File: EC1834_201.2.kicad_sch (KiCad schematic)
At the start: 69 parts, among them X4 Lautsprecher, X7 DB9_Female

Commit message: Page 1 & 2 connected Hierarchival connections created and tested
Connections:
- net 0: no longer R15.6 (R3.2)
- net 1: no longer R15.1 (R1.1)
- net 2: no longer R15.3 (R2.1)
- net 3: no longer R15.7 (R4.1)
- net 4: no longer R14.4 (R2.2)
- net 5: no longer R14.7 (R4.1)
- net 6: no longer R14.2 (R1.2)
- net 7: no longer R14.6 (R3.2)
- net A1: now also D85.14 (A3)
- net A14: now also D86.10 (B2)
- net A15: now also D86.6 (B1)
- net A16: now also D86.13 (B3)
- net A2: now also D85.5 (A1)
- net A3: now also D85.2 (A0)
- net A4: now also D85.11 (A2)
- net A5: now also D86.2 (A0)
- net A6: now also D86.11 (A2)
- net A7: now also D86.5 (A1)
- net A9: now also D85.13 (B3)
- net PS3:1: now also D60.10 (S), R52.8 (R7.2)
- net ~{DACK0}: now also D58.1 (R)
- net ~{MEMR}: now also BR1.1 (A)
- net ~{RAMADRSEL}: now also D87.9 (A4), D88.3 (Y1)
- net ADRSEL: now reaches D58.9, D67.2 (D), D85.1 (WS), D86.1 (WS)
- net A12: now reaches D85.10 (B2)
- net A11: now reaches D85.3 (B0)
- net A10: now reaches D85.6 (B1)
- net A13: now reaches D86.3 (B0)
- net at D57.10 (B3), D57.12 (A4), D57.13 (B4)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: now also D58.3 (C)
- net ~{MEMW}: now reaches D60.12 (D)
- net 5PW1: now reaches D60.13 (R)
- net 5PW1: now also D58.10 (S), D58.4 (S), D67.4 (S)
- net at D58.2 (D), D69.8 (Y3): now also D67.1 (R), D70.1 (A1), D70.4 (A2)
- net OSC1: now reaches D57.1 (A1), D57.2 (B1)
- net OSC: now reaches D57.8 (Y3)
- net at D67.5, D69.1 (A1): now also D69.12 (A4)
- new net MEM0: R15.6 (R3.2)
- new net MEM1: R15.1 (R1.1)
- new net MEM2: R15.3 (R2.1)
- new net MEM3: R15.7 (R4.1)
- new net MEM4: R14.4 (R2.2)
- new net MEM5: R14.7 (R4.1)
- new net MEM6: R14.2 (R1.2)
- new net MEM7: R14.6 (R3.2)
- no-connect marks 44 -> 45

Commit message: Completed BUS Final checks required
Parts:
- BR1, WD4, WD5: footprint (none) -> Resistor_THT:R_Axial_DIN0204_L3.6mm_D1.6mm_P7.62mm_Horizontal
- D10, D13, D16, D34, D37, D39, D47, D5, D52, D57, D58, D59, D60, D62, D63, D67, D68, D69, D70, D71, D72, D82, D87, D88, D90: footprint (none) -> Package_DIP:DIP-14_W7.62mm
- D100, D101, D115, D116: footprint (none) -> Package_DIP:DIP-28_W15.24mm
- D111, D112, D30, D31, D44: footprint (none) -> Package_DIP:DIP-20_W7.62mm
- D65, D66, D85, D86: footprint (none) -> Package_DIP:DIP-16_W7.62mm
- E4, X4: footprint (none) -> Connector_PinHeader_2.54mm:PinHeader_1x02_P2.54mm_Vertical
- L1: footprint (none) -> Package_DIP:DIP-8_W7.62mm
- PS3: footprint (none) -> Connector_PinHeader_2.54mm:PinHeader_1x09_P2.54mm_Vertical
- PS4: footprint (none) -> Connector_PinHeader_2.54mm:PinHeader_1x03_P2.54mm_Vertical
- X7: footprint (none) -> Connector_Dsub:DSUB-9_Female_Horizontal_P2.77x2.84mm_EdgePinOffset9.90mm_Housed_MountingHolesOffset11.32mm
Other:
- company: (none) -> Mario Gögel 2022
- title: EC1834_201.2 -> EC1834 Hauptplatine 201.2

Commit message: Small corrections on Page 201.1
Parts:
- WD4: value SolderJumper_2_Bridged -> SolderJumper_2_Open; symbol Jumper:SolderJumper_2_Bridged -> Jumper:SolderJumper_2_Open
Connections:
- net ~{MEMR} is gone; now on net PS4:1: BR1.1 (A), D60.3 (C)
- net ~{MEMADRSEL}: now also D90.3 (Y1), WD5.2 (B)
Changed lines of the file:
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@@
     (stroke (width 0) (type default) (color 0 0 0 0))
   )
-  (bus (pts (xy 134.62 271.78) (xy 134.62 275.59))
-    (stroke (width 0.5) (type default) (color 0 0 0 0))
-  )
   (wire (pts (xy 299.72 364.49) (xy 290.83 364.49))
     (stroke (width 0) (type default) (color 0 0 0 0))
@@
     (stroke (width 2) (type default) (color 0 0 0 0))
   )
-  (bus (pts (xy 138.43 223.52) (xy 138.43 226.06))
-    (stroke (width 0.5) (type default) (color 0 0 0 0))
-  )
   (wire (pts (xy 82.55 125.73) (xy 82.55 129.54))
     (stroke (width 0) (type default) (color 0 0 0 0))
@@
     (effects (font (size 1.27 1.27)) (justify left bottom))
   )
+  (label "~{MEMR}" (at 212.09 123.19 0)
+    (effects (font (size 1.27 1.27)) (justify left bottom))
+  )
   (label "~{OCHCK}" (at 172.72 316.23 0)
     (effects (font (size 1.27 1.27)) (justify left bottom))
@@
     (effects (font (size 1.27 1.27)) (justify left bottom))
   )
+  (label "~{MEMADRSEL}" (at 125.73 179.07 0)
+    (effects (font (size 1.27 1.27)) (justify left bottom))
+  )
   (label "PB1" (at 229.87 321.31 0)
     (effects (font (size 1.27 1.27)) (justify left bottom))
@@
   (symbol (lib_id "robotron_ec1834:DS8286D-D111") (at 156.21 217.17 0) (unit 1)
     (in_bom yes) (on_board yes)
-    (property "Reference" "D44" (id 0) (at 156.21 204.9018 0))
+    (property "Reference" "D44" (id 0) (at 156.21 231.14 0))
     (property "Value" "DS8286D-D111" (id 1) (at 156.21 233.68 0)
       (effects (font (size 1.27 1.27)) hide)
@@
   (symbol (lib_id "robotron_ec1834:DL374") (at 156.21 250.19 0) (unit 1)
     (in_bom yes) (on_board yes)
-    (property "Reference" "D30" (id 0) (at 156.21 233.045 0))
+    (property "Reference" "D30" (id 0) (at 156.21 261.62 0))
     (property "Value" "DL374" (id 1) (at 156.21 235.3564 0))
     (property "Footprint" "Package_DIP:DIP-20_W7.62mm" (id 2) (at 156.21 252.73 0)
@@
   (symbol (lib_id "robotron_ec1834:DL374") (at 156.21 280.67 0) (unit 1)
     (in_bom yes) (on_board yes)
-    (property "Reference" "D31" (id 0) (at 156.21 263.525 0))
+    (property "Reference" "D31" (id 0) (at 156.21 292.1 0))
     (property "Value" "DL374" (id 1) (at 156.21 265.8364 0))
     (property "Footprint" "Package_DIP:DIP-20_W7.62mm" (id 2) (at 156.21 283.21 0)
@@
     (pin "1")
   )
-  (symbol (lib_id "Jumper:SolderJumper_2_Bridged") (at 215.9 215.9 0) (unit 1)
+  (symbol (lib_id "Jumper:SolderJumper_2_Open") (at 215.9 215.9 0) (unit 1)
     (in_bom yes) (on_board yes)
     (property "Reference" "WD4" (id 0) (at 215.9 213.36 0))
-    (property "Value" "SolderJumper_2_Bridged" (id 1) (at 215.9 213.8481 0)
+    (property "Value" "SolderJumper_2_Open" (id 1) (at 215.9 213.8481 0)
       (effects (font (size 1.27 1.27)) hide)
     )

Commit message: Updated footprints Updated PCB
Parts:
- R17, R18, R24, R25, R53, R54: footprint Resistor_THT:R_Axial_DIN0309_L9.0mm_D3.2mm_P12.70mm_Horizontal -> EC1834-Board:R_Axial_L9.0mm_D1.8mm_P12.70mm_Horizontal
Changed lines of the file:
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@@
     (property "Reference" "R17" (id 0) (at 102.87 173.8122 90))
     (property "Value" "4k7" (id 1) (at 102.87 176.1236 90))
-    (property "Footprint" "Resistor_THT:R_Axial_DIN0309_L9.0mm_D3.2mm_P12.70mm_Horizontal" (id 2) (at 102.87 177.292 90)
+    (property "Footprint" "EC1834-Board:R_Axial_L9.0mm_D1.8mm_P12.70mm_Horizontal" (id 2) (at 102.87 177.292 90)
       (effects (font (size 1.27 1.27)) hide)
     )
@@
     (property "Reference" "R18" (id 0) (at 363.22 185.42 90))
     (property "Value" "30" (id 1) (at 363.22 182.88 90))
-    (property "Footprint" "Resistor_THT:R_Axial_DIN0309_L9.0mm_D3.2mm_P12.70mm_Horizontal" (id 2) (at 363.22 181.102 90)
+    (property "Footprint" "EC1834-Board:R_Axial_L9.0mm_D1.8mm_P12.70mm_Horizontal" (id 2) (at 363.22 181.102 90)
       (effects (font (size 1.27 1.27)) hide)
     )
@@
     (property "Reference" "R24" (id 0) (at 274.32 381 90))
     (property "Value" "1k" (id 1) (at 275.59 375.92 90))
-    (property "Footprint" "Resistor_THT:R_Axial_DIN0309_L9.0mm_D3.2mm_P12.70mm_Horizontal" (id 2) (at 277.368 375.92 90)
+    (property "Footprint" "EC1834-Board:R_Axial_L9.0mm_D1.8mm_P12.70mm_Horizontal" (id 2) (at 277.368 375.92 90)
       (effects (font (size 1.27 1.27)) hide)
     )
@@
     (property "Reference" "R25" (id 0) (at 267.97 381 90))
     (property "Value" "1k" (id 1) (at 269.24 375.92 90))
-    (property "Footprint" "Resistor_THT:R_Axial_DIN0309_L9.0mm_D3.2mm_P12.70mm_Horizontal" (id 2) (at 271.018 375.92 90)
+    (property "Footprint" "EC1834-Board:R_Axial_L9.0mm_D1.8mm_P12.70mm_Horizontal" (id 2) (at 271.018 375.92 90)
       (effects (font (size 1.27 1.27)) hide)
     )
@@
     (property "Reference" "R53" (id 0) (at 310.9722 107.95 90))
     (property "Value" "100" (id 1) (at 313.2836 107.95 90))
-    (property "Footprint" "Resistor_THT:R_Axial_DIN0309_L9.0mm_D3.2mm_P12.70mm_Horizontal" (id 2) (at 314.452 107.95 90)
+    (property "Footprint" "EC1834-Board:R_Axial_L9.0mm_D1.8mm_P12.70mm_Horizontal" (id 2) (at 314.452 107.95 90)
       (effects (font (size 1.27 1.27)) hide)
     )
@@
     (property "Reference" "R54" (id 0) (at 205.74 219.71 90))
     (property "Value" "100" (id 1) (at 205.74 224.79 90))
-    (property "Footprint" "Resistor_THT:R_Axial_DIN0309_L9.0mm_D3.2mm_P12.70mm_Horizontal" (id 2) (at 205.74 220.472 90)
-      (effects (font (size 1.27 1.27)) hide)
-    )
+    (property "Footprint" "EC1834-Board:R_Axial_L9.0mm_D1.8mm_P12.70mm_Horizontal" (id 2) (at 205.74 220.472 90)
+      (effects (font (size 1.27 1.27)) hide)
+    )

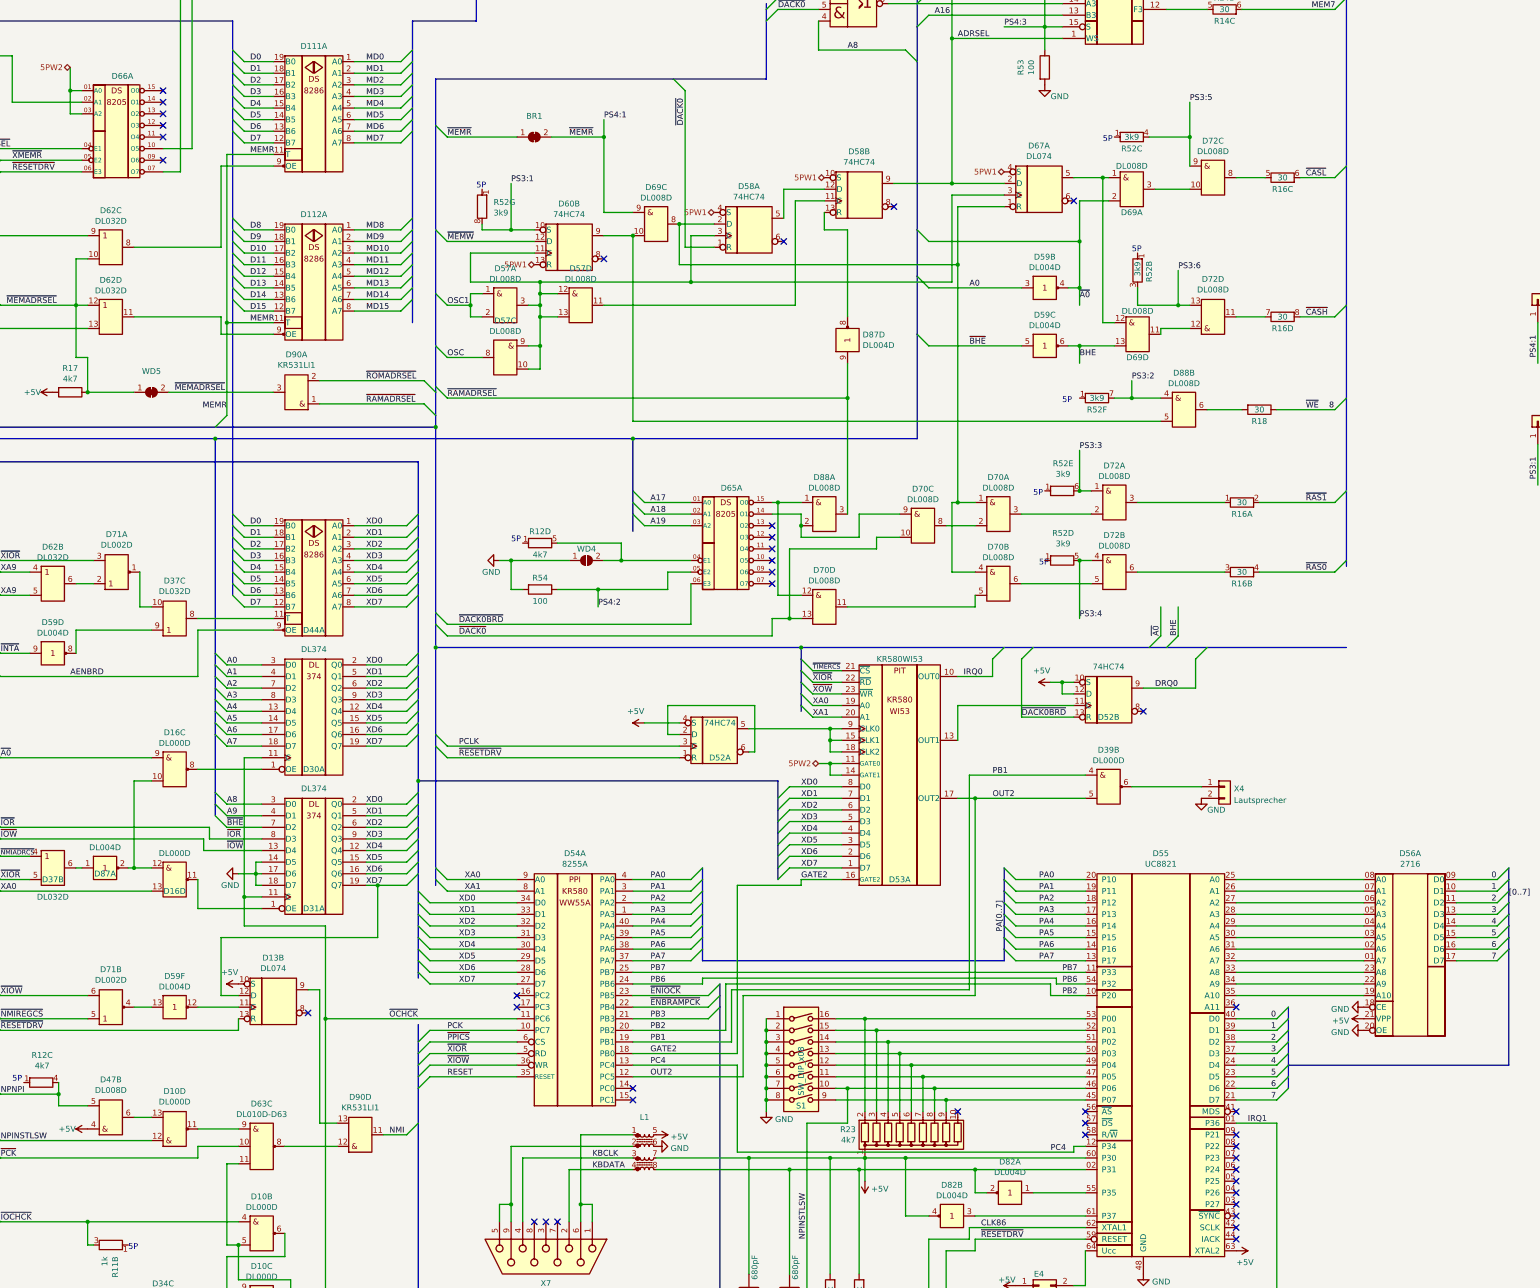
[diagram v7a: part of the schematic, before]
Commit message: Updated some symbol pins no more error on PCB import due to leading zero on pin number also fixed missing network connections added unused pin connections on bus connectors
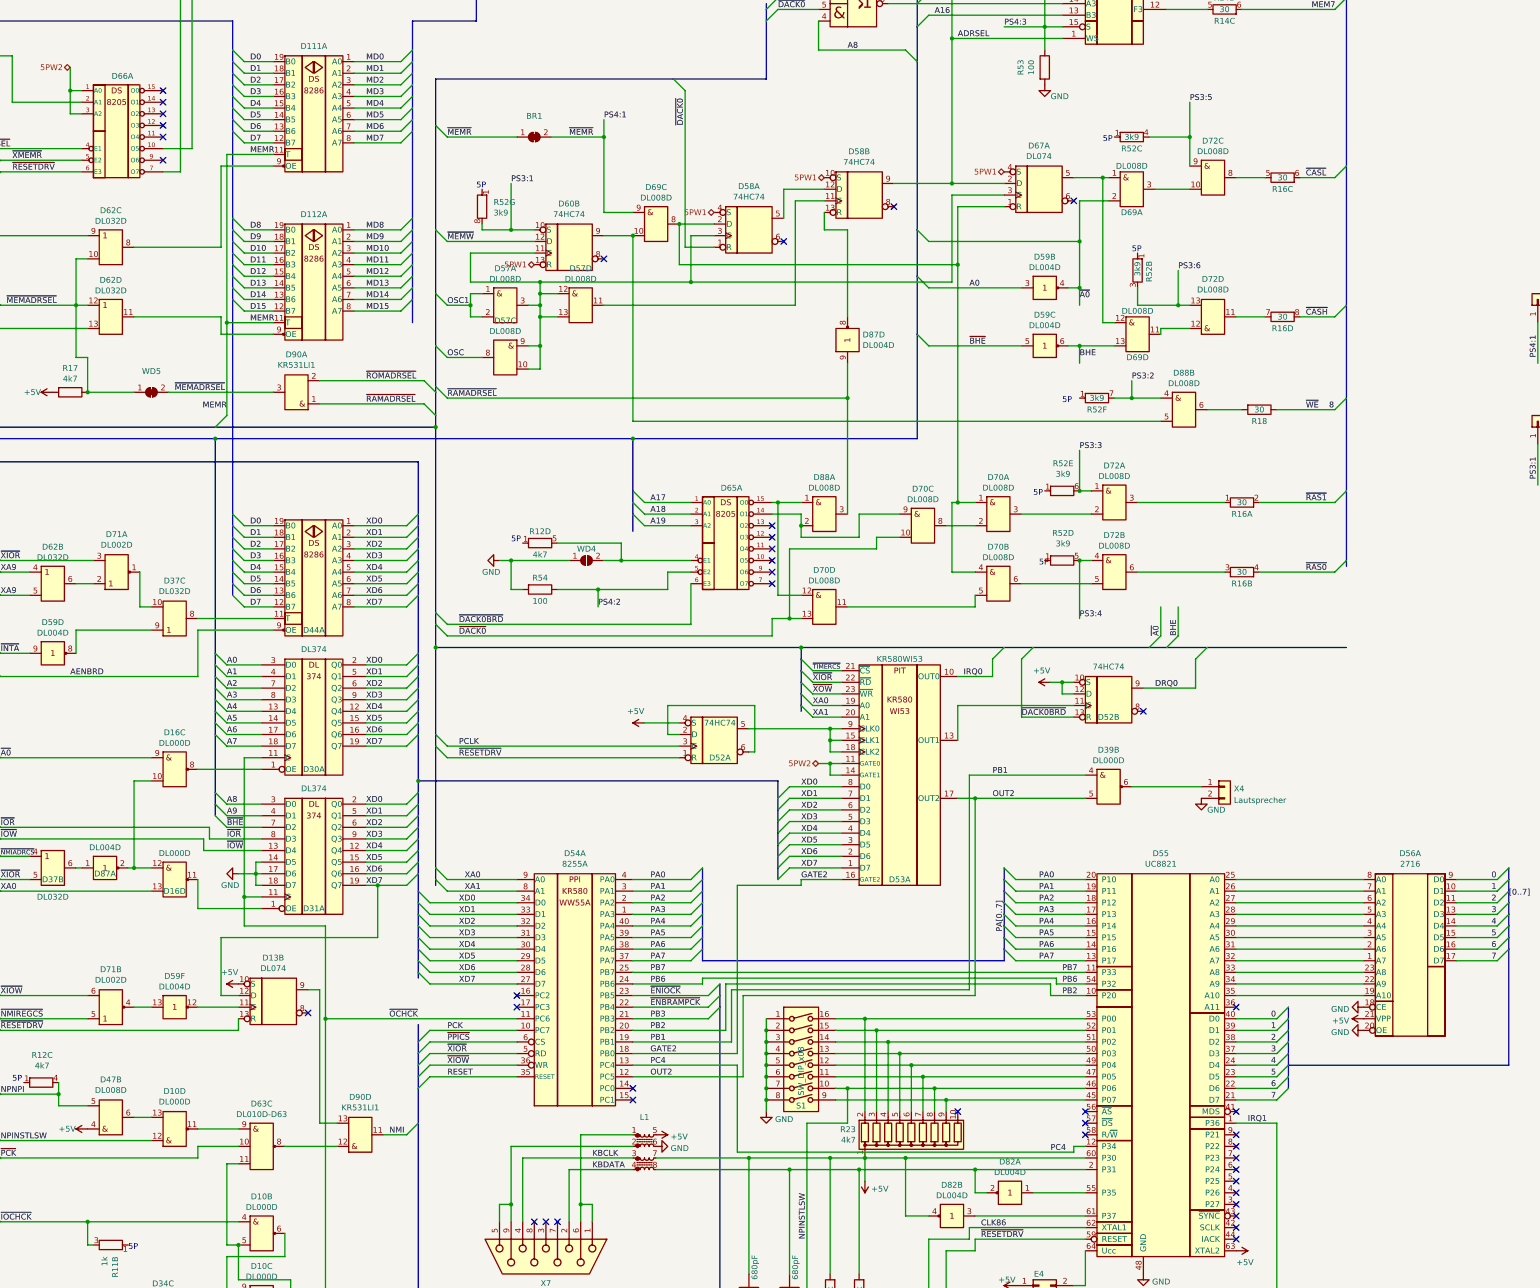
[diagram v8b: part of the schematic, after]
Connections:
- net 0: now also D56.9 (D0); no longer D56.09 (D0)
- net 5PW2: now also D66.1 (A0), D66.3 (A2); no longer D66.01 (A0), D66.03 (A2)
- net A14: now also D66.2 (A1); no longer D66.02 (A1)
- net A17: now also D65.1 (A0); no longer D65.01 (A0)
- net A18: now also D65.2 (A1); no longer D65.02 (A1)
- net A19: now also D65.3 (A2); no longer D65.03 (A2)
- net IRQ1: now also D55.1 (P36); no longer D55.01 (P36)
- net PS4:2: now also D65.5 (E2); no longer D65.05 (E2)
- net ~{CSROM1}: now also D66.7 (O7); no longer D66.07 (O7)
- net ~{DACK0BRD}: now also D65.6 (E3); no longer D65.06 (E3)
- net ~{RESETDRV}: now also D66.6 (E3); no longer D66.06 (E3)
- net ~{ROMADRSEL}: now also D66.4 (E1); no longer D66.04 (E1)
- net ~{XMEMR}: now also D66.5 (E2); no longer D66.05 (E2)
- net at C8.1, D82.2 (Y1), L1.8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: now also D55.2 (P31); no longer D55.02 (P31)
- net at D55.25 (A0): now also D56.8 (A0); no longer D56.08 (A0)
- net at D55.26 (A1): now also D56.7 (A1); no longer D56.07 (A1)
- net at D55.27 (A2): now also D56.6 (A2); no longer D56.06 (A2)
- net at D55.28 (A3): now also D56.5 (A3); no longer D56.05 (A3)
- net at D55.29 (A4): now also D56.4 (A4); no longer D56.04 (A4)
- net at D55.30 (A5): now also D56.3 (A5); no longer D56.03 (A5)
- net at D55.31 (A6): now also D56.2 (A6); no longer D56.02 (A6)
- net at D55.32 (A7): now also D56.1 (A7); no longer D56.01 (A7)
- net at R12.5 (R4.2), WD4.2 (B): now also D65.4 (E1); no longer D65.04 (E1)
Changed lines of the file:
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@@
       (effects (font (size 1.27 1.27)) hide)
     )
-    (pin "01")
-    (pin "02")
-    (pin "03")
-    (pin "04")
-    (pin "05")
-    (pin "06")
-    (pin "07")
-    (pin "09")
+    (pin "1")
     (pin "10")
     (pin "11")
@@
     (pin "14")
     (pin "15")
+    (pin "2")
+    (pin "3")
+    (pin "4")
+    (pin "5")
+    (pin "6")
+    (pin "7")
+    (pin "9")
     (pin "16")
     (pin "8")
@@
       (effects (font (size 1.27 1.27)) hide)
     )
-    (pin "01")
-    (pin "02")
-    (pin "03")
-    (pin "04")
-    (pin "05")
-    (pin "06")
-    (pin "07")
-    (pin "08")
-    (pin "09")
+    (pin "1")
     (pin "10")
     (pin "11")
@@
     (pin "18")
     (pin "19")
+    (pin "2")
     (pin "20")
     (pin "21")
@@
     (pin "28")
     (pin "29")
+    (pin "3")
     (pin "30")
     (pin "31")
@@
     (pin "38")
     (pin "39")
+    (pin "4")
     (pin "40")
     (pin "41")
@@
     (pin "48")
     (pin "49")
+    (pin "5")
     (pin "50")
     (pin "51")
@@
     (pin "58")
     (pin "59")
+    (pin "6")
     (pin "60")
     (pin "61")
@@
     (pin "63")
     (pin "64")
+    (pin "7")
+    (pin "8")
+    (pin "9")
   )
   (symbol (lib_id "RFT_Digitalschaltkreise:DL000D") (at 125.73 261.62 0) (unit 3)
@@
       (effects (font (size 1.27 1.27)) hide)
     )
-    (pin "01")
-    (pin "02")
-    (pin "03")
-    (pin "04")
-    (pin "05")
-    (pin "06")
-    (pin "07")
-    (pin "08")
-    (pin "09")
+    (pin "1")
     (pin "10")
     (pin "11")
@@
     (pin "18")
     (pin "19")
+    (pin "2")
     (pin "20")
     (pin "21")
     (pin "22")
     (pin "23")
+    (pin "3")
+    (pin "4")
+    (pin "5")
+    (pin "6")
+    (pin "7")
+    (pin "8")
+    (pin "9")
     (pin "12")
     (pin "24")
@@
     (pin "7")
   )
-  (symbol (lib_id "robotron_ec1834:DS8205") (at 246.38 212.09 0) (unit 1)
+  (symbol (lib_name "DS8205_1") (lib_id "robotron_ec1834:DS8205") (at 246.38 212.09 0) (unit 1)
     (in_bom yes) (on_board yes)
     (property "Reference" "D65" (id 0) (at 247.65 200.025 0))
@@
       (effects (font (size 1.27 1.27)) hide)
     )
-    (pin "01")
-    (pin "02")
-    (pin "03")
-    (pin "04")
-    (pin "05")
-    (pin "06")
-    (pin "07")
-    (pin "09")
+    (pin "1")
     (pin "10")
     (pin "11")
@@
     (pin "14")
     (pin "15")
+    (pin "2")
+    (pin "3")
+    (pin "4")
+    (pin "5")
+    (pin "6")
+    (pin "7")
+    (pin "9")
     (pin "16")
     (pin "8")
